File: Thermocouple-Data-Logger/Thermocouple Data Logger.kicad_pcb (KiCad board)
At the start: 4 copper layers, 75 x 85 mm, 149 parts, among them J0 Power, J1 Micro_SD_Card_Det, J2 Probe 1, J3 Probe 2, J4 Probe 3, J5 Probe 4, J6 ISP, SW0 Power, SW1 Display, SW2 Reset, SW3 Select/Calibrate, SW4 Cycle/Menu, SW5 SW_DIP_x04, U0 ATMEGA324PA-MU, U1 LT1763-3.3, U10 74HC595, U11 HDSP-521E-Display, U12 HDSP-521E-Display, U13 4050, U2 MAX31856, U3 MAX31856, U4 MAX31856, U5 MAX31856, U6 74HC595, U7 74HC595, U8 74HC595, U9 74HC595, Y0 10MHz, Y1 32.768KHz

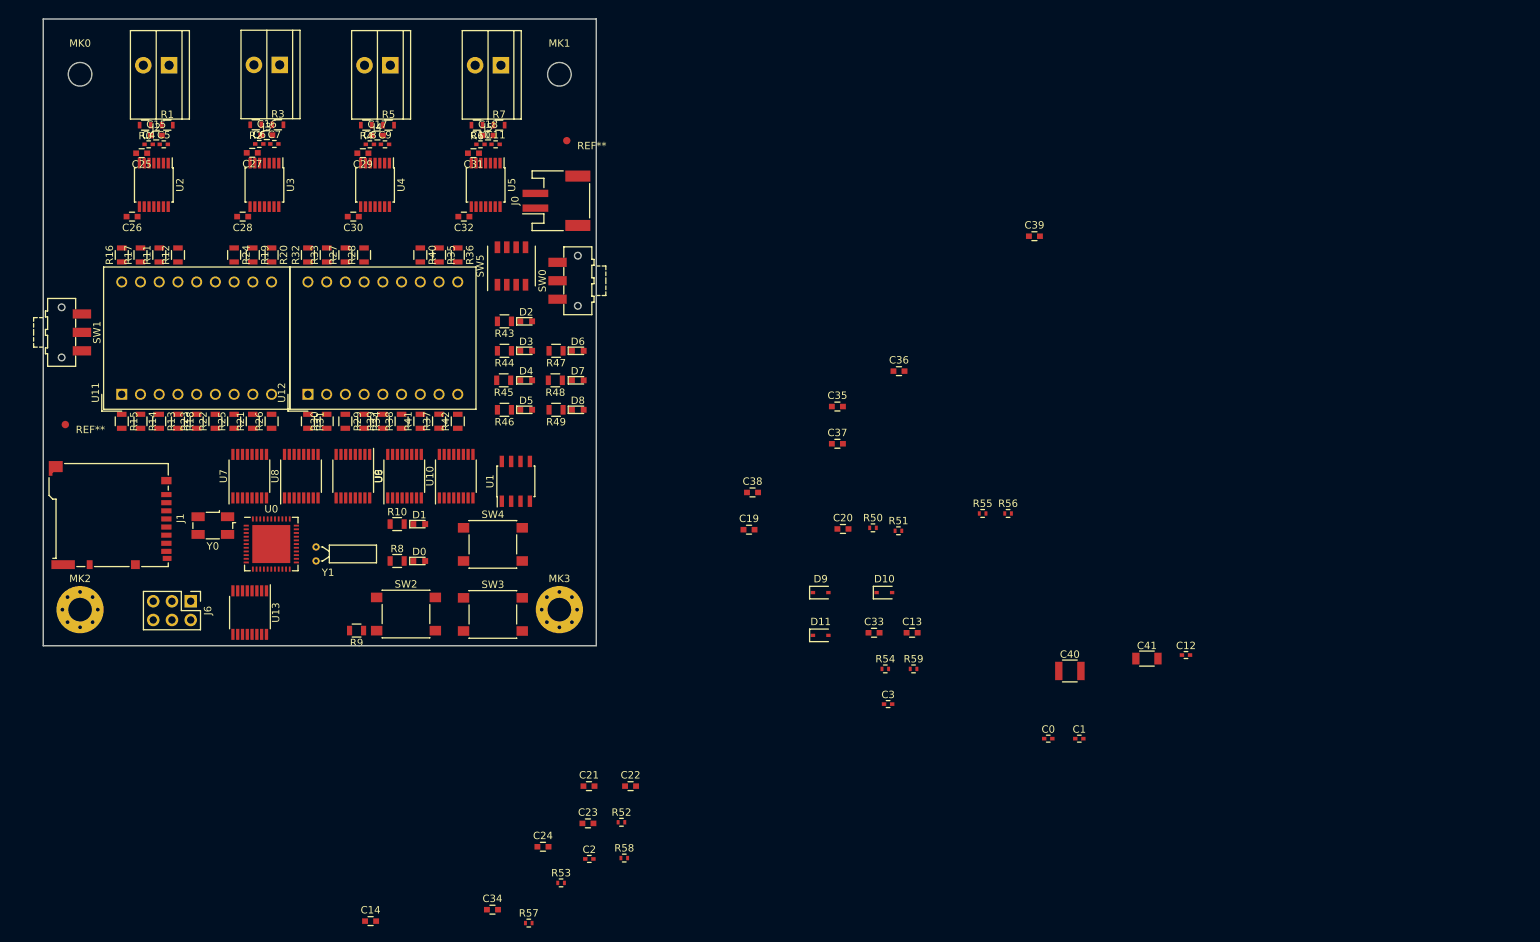
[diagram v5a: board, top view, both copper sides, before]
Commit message: Changed capacitor values and component layout
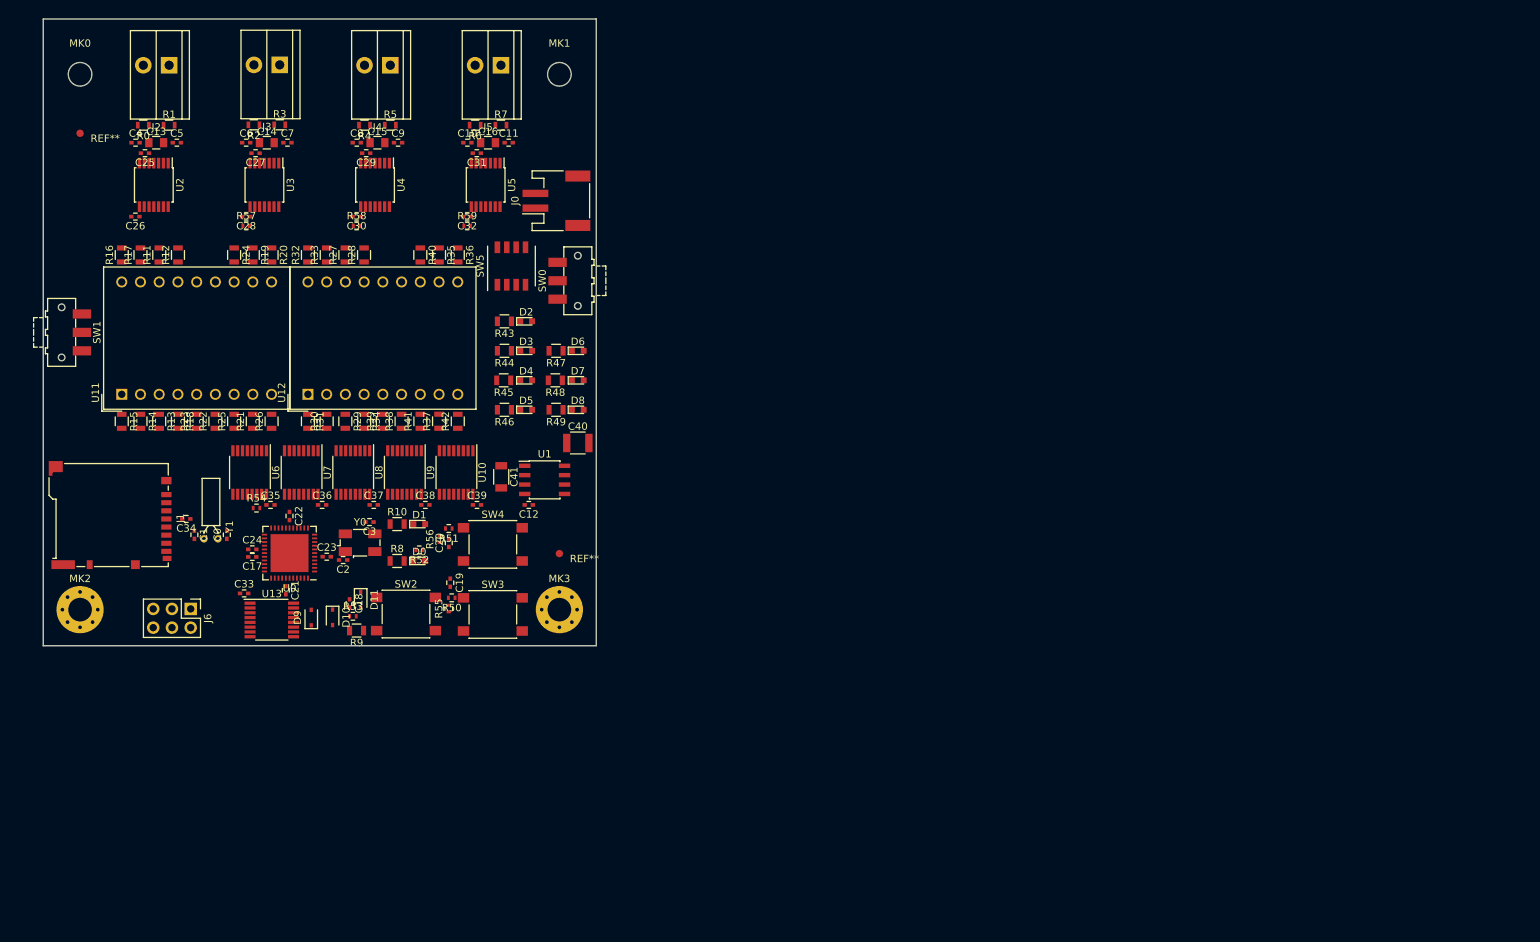
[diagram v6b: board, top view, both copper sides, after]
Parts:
- C13, C14, C15, C16: footprint Capacitors_SMD:C_0603 -> Capacitors_SMD:C_0805
- C17, C18, C19, C20: footprint Capacitors_SMD:C_0603 -> Capacitors_SMD:C_0402
- C21, C22, C23, C24, C25, C26, C27, C28, C29, C30, C31, C32, C33, C34, C35, C36, C37, C38, C39: value 0.33uF -> 0.1uF; footprint Capacitors_SMD:C_0603 -> Capacitors_SMD:C_0402
- moved C1 123.2 mm to (85.5, 87.5), turned to 270 degrees
- moved C13 122.2 mm to (80.3, 34.3)
- moved C0 114.8 mm to (89.9, 87.5), turned to 90 degrees
- moved C14 106.5 mm to (95.3, 34.3)
- moved R57 102.0 mm to (92.5, 45.5)
- moved R58 93.1 mm to (107.5, 45.5)
- moved C12 91.4 mm to (130.8, 83.4), turned to 180 degrees
- moved C41 91.0 mm to (127.1, 79.6), turned to 270 degrees
- moved R54 88.0 mm to (93.9, 83.8)
- moved C33 85.6 mm to (92.2, 95.4)
- moved R59 85.3 mm to (122.5, 45.5)
- moved C39 83.9 mm to (123.8, 83.4)
- moved C36 80.3 mm to (102.8, 83.4)
- moved C35 78.0 mm to (95.8, 83.4)
- moved R56 77.1 mm to (118.8, 88.0), turned to 90 degrees
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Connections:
- C13 pad 2: GND -> Net-(C13-Pad2)
- C14 pad 1: GND -> Net-(C14-Pad1)
- C14 pad 2: RESET -> Net-(C14-Pad2)
- C16 pad 1: Net-(C16-Pad1) -> Net-(C10-Pad2)
- C16 pad 2: Net-(C16-Pad2) -> Net-(C11-Pad1)
- C17 pad 2: Net-(C17-Pad2) -> GND
- C18 pad 1: Net-(C10-Pad2) -> GND
- C18 pad 2: Net-(C11-Pad1) -> RESET
- C4 pad 2: Net-(C15-Pad1) -> Net-(C13-Pad1)
- C5 pad 1: Net-(C15-Pad2) -> Net-(C13-Pad2)
- C6 pad 2: Net-(C16-Pad1) -> Net-(C14-Pad1)
- C7 pad 1: Net-(C16-Pad2) -> Net-(C14-Pad2)
- C8 pad 2: Net-(C17-Pad1) -> Net-(C15-Pad1)
- C9 pad 1: Net-(C17-Pad2) -> Net-(C15-Pad2)
- R0 pad 1: Net-(C15-Pad1) -> Net-(C13-Pad1)
- R1 pad 1: Net-(C15-Pad2) -> Net-(C13-Pad2)
- R2 pad 1: Net-(C16-Pad1) -> Net-(C14-Pad1)
- R3 pad 1: Net-(C16-Pad2) -> Net-(C14-Pad2)
- R4 pad 1: Net-(C17-Pad1) -> Net-(C15-Pad1)
- R5 pad 1: Net-(C17-Pad2) -> Net-(C15-Pad2)
- U0 pad 29: Net-(C13-Pad1) -> Net-(C17-Pad1)
- U2 pad 3: Net-(C15-Pad2) -> Net-(C13-Pad2)
- U2 pad 4: Net-(C15-Pad1) -> Net-(C13-Pad1)
- U3 pad 3: Net-(C16-Pad2) -> Net-(C14-Pad2)
- U3 pad 4: Net-(C16-Pad1) -> Net-(C14-Pad1)
- U4 pad 3: Net-(C17-Pad2) -> Net-(C15-Pad2)
- U4 pad 4: Net-(C17-Pad1) -> Net-(C15-Pad1)
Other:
- net class Default: clearance 0.2 -> 0.1; via_dia 0.8 -> 0.6; via_drill 0.4 -> 0.3
- net class Power added: clearance 0.2, trace_width 0.25, via_dia 0.6, via_drill 0.3
- rule trace_clearance: 0.2 -> 0.1

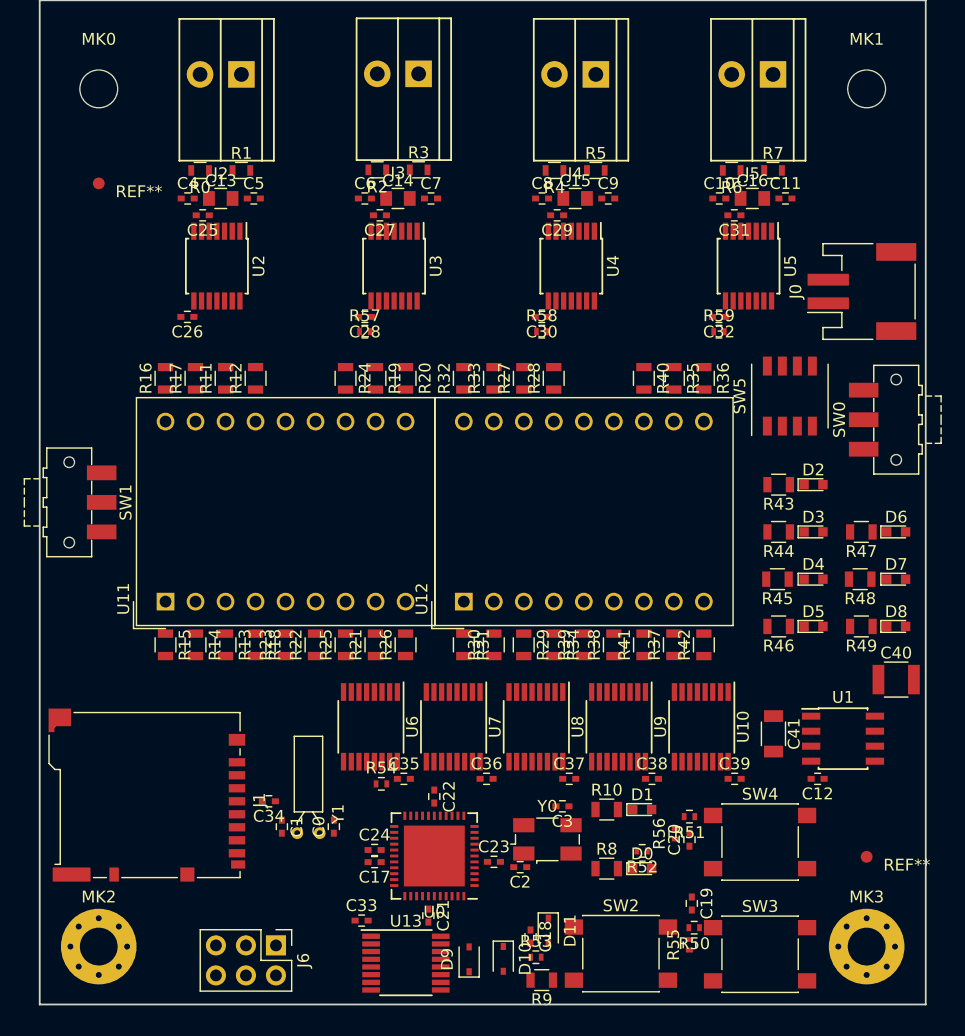
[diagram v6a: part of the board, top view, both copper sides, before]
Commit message: Started laying down traces
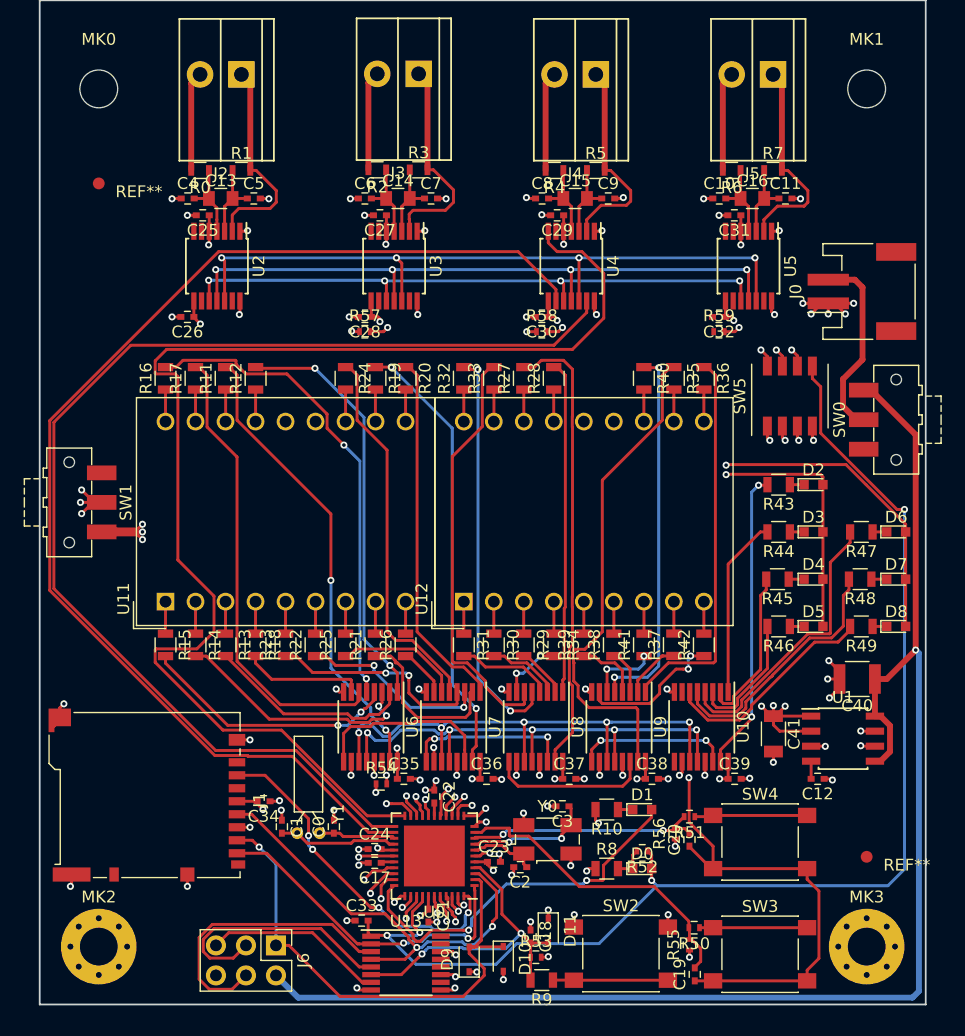
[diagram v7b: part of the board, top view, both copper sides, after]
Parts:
- moved C19 6.01 mm to (120.5, 100.0), turned to 90 degrees
- moved C40 3.30 mm to (134.2, 75.0), turned to 180 degrees
- moved C34 0.45 mm to (84.0, 85.3)
- moved C24 0.08 mm to (93.3, 89.3)
- moved C17 0.06 mm to (93.4, 90.5)
- turned R10 to 180 degrees
- turned R30 to 270 degrees
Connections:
- U8 pad 11: (no net) -> SRCLK
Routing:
- net +5V: track 0.00 -> 121.6 mm, vias 0 -> 1
- net GND: track 0.00 -> 118.1 mm, vias 0 -> 88
- net DD: track 0.00 -> 116.1 mm, vias 0 -> 18
- net DRDY3: track 0.00 -> 109.2 mm
- net DEBUG: track 0.00 -> 107.0 mm, vias 0 -> 4
- net CS3: track 0.00 -> 103.1 mm
- net FAULT3: track 0.00 -> 101.2 mm
- net MOSI2: track 0.00 -> 62.2 mm, vias 0 -> 5
- net MISO2: track 0.00 -> 56.9 mm, vias 0 -> 5
- net SCK2: track 0.00 -> 54.0 mm, vias 0 -> 5
- net SRCLK: track 0.00 -> 47.7 mm, vias 0 -> 6
- net MISO1: track 0.00 -> 43.9 mm, vias 0 -> 1
- net RCLK: track 0.00 -> 43.6 mm, vias 0 -> 6
- net /Thermocouple/VCC2: track 0.00 -> 42.7 mm, vias 0 -> 5
- net Net-(R35-Pad1): track 0.00 -> 42.3 mm
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- added copper zone on In2.Cu, net /Thermocouple/VCC2
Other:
- net class High Power added: clearance 0.2, trace_width 0.5, via_dia 0.6, via_drill 0.3

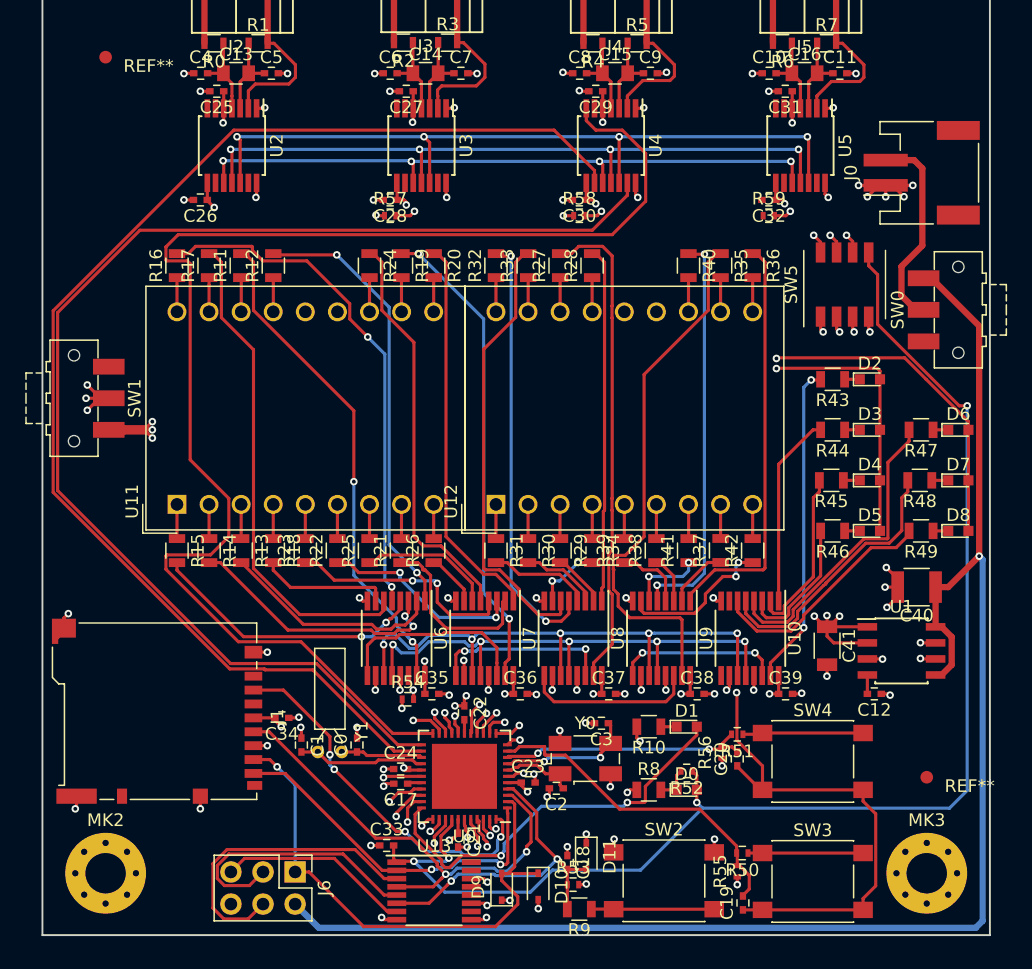
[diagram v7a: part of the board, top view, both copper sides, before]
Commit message: Finished routing all traces
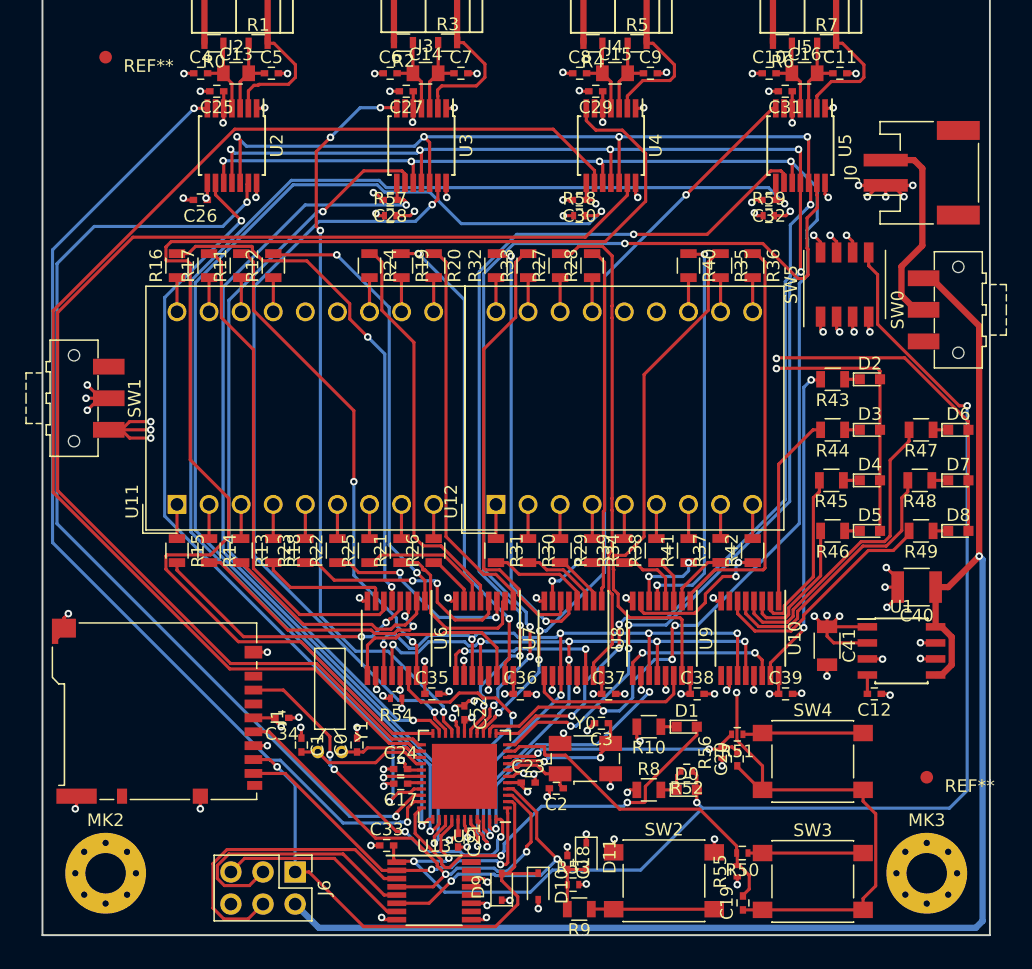
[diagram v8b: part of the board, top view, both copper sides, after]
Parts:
- moved R54 0.93 mm to (93.0, 83.8), turned to 180 degrees
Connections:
- U0 pad 31: CS1 -> FAULT1
- U2 pad 13: CS1 -> FAULT1
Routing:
- net /Thermocouple/VCC4: track 14.1 -> 115.8 mm
- net /Thermocouple/VCC3: track 28.0 -> 116.1 mm
- net FAULT1: track 0.00 -> 78.5 mm, vias 0 -> 2
- net DRDY1: track 2.43 -> 79.8 mm, vias 1 -> 2
- net FAULT4: track 1.89 -> 75.2 mm, vias 1 -> 4
- net /Thermocouple/VCC2: track 42.7 -> 111.1 mm
- net CS4: track 2.57 -> 68.4 mm, vias 1 -> 4
- net SCK2: track 54.0 -> 116.5 mm, vias 5 -> 7
- net FAULT2: track 2.04 -> 61.5 mm, vias 1 -> 2
- net CS2: track 2.68 -> 61.7 mm, vias 1 -> 2
- net DRDY2: track 1.86 -> 59.8 mm, vias 1 -> 4
- net MISO2: track 56.9 -> 114.3 mm, vias 5 -> 8
- net DRDY4: track 2.07 -> 59.5 mm, vias 1 -> 4
- net CS1: track 5.83 -> 63.0 mm
- net MOSI2: track 62.2 -> 119.3 mm, vias 5 -> 8
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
